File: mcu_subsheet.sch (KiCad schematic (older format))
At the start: 22 parts

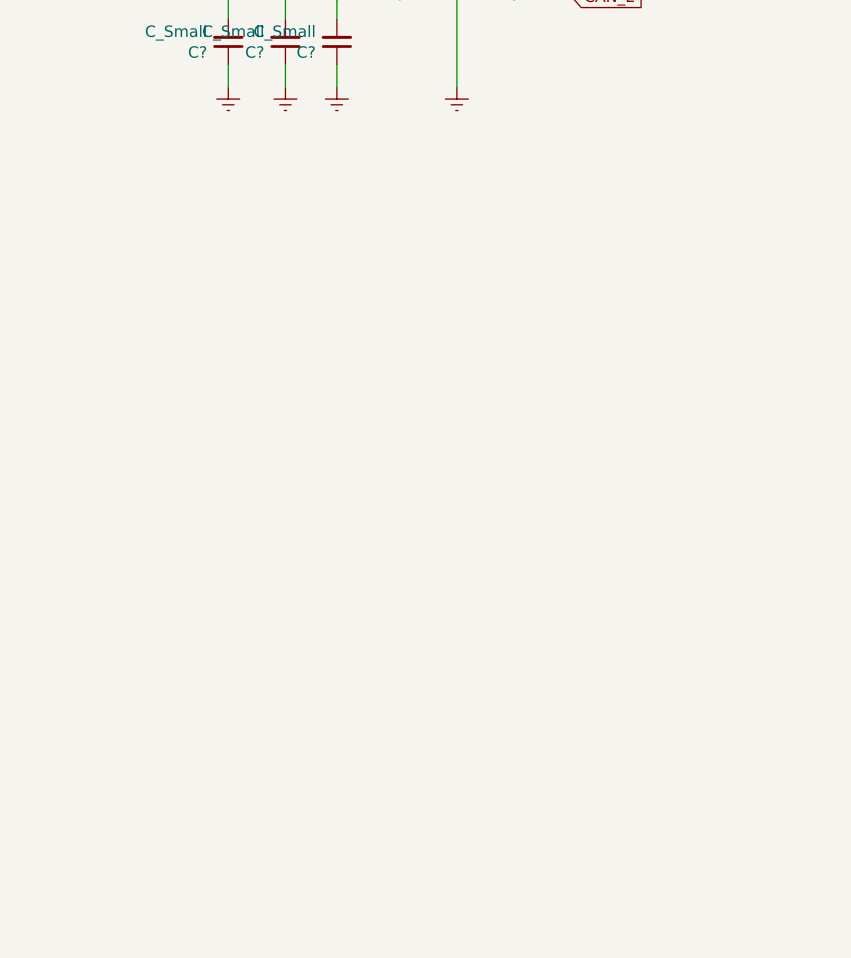
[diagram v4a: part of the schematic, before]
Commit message: [debug]: add swd connector
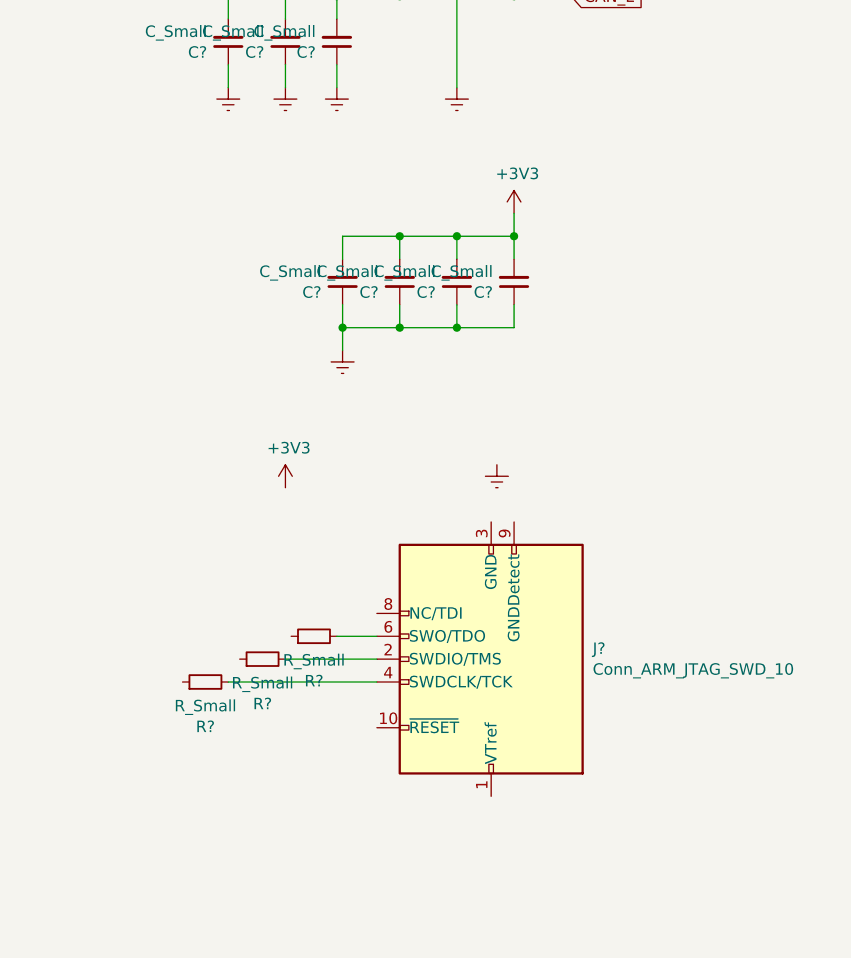
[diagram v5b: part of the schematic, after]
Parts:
- added C? (x4): C_Small, symbol Device:C_Small
- added J?: Conn_ARM_JTAG_SWD_10, symbol Connector:Conn_ARM_JTAG_SWD_10
- added R? (x3): R_Small, symbol Device:R_Small
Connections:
- net +3V3: now also C?.2, C?.2, C?.2, C?.2
- net Earth: now also C?.1, C?.1, C?.1, C?.1
- new net: J?.2 (SWDIO/TMS), R?.2
- new net: J?.3 (GND), J?.5 (GND)
- new net: J?.4 (SWDCLK/TCK), R?.2
- new net: J?.6 (SWO/TDO), R?.2
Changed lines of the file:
@@
 Wire Wire Line
 	7150 2050 7150 2150
+$Comp
+L Connector:Conn_ARM_JTAG_SWD_10 J?
+U 1 1 61E3A5F4
+P 9650 4750
+F 0 "J?" H 9206 4704 50  0000 R CNN
+F 1 "Conn_ARM_JTAG_SWD_10" H 9206 4795 50  0000 R CNN
+F 2 "" H 9650 4750 50  0001 C CNN
+F 3 "http://infocenter.arm.com/help/topic/com.arm.doc.ddi0314h/DDI0314H_coresight_components_trm.pdf" V 9300 3500 50  0001 C CNN
+	1    9650 4750
+	-1   0    0    1
+$EndComp
+$Comp
+L power:+3V3 #PWR?
+U 1 1 61E4B09B
+P 8750 4000
+F 0 "#PWR?" H 8750 3850 50  0001 C CNN
+F 1 "+3V3" H 8765 4173 50  0000 C CNN
+F 2 "" H 8750 4000 50  0001 C CNN
+F 3 "" H 8750 4000 50  0001 C CNN
+	1    8750 4000
+	1    0    0    -1
+$EndComp
+Wire Wire Line
+	8975 4650 9150 4650
+$Comp
+L Device:R_Small R?
+U 1 1 61E51799
+P 8875 4650
+F 0 "R?" V 8679 4650 50  0000 C CNN
+F 1 "R_Small" V 8770 4650 50  0000 C CNN
+F 2 "" H 8875 4650 50  0001 C CNN
+F 3 "~" H 8875 4650 50  0001 C CNN
+	1    8875 4650
+	0    -1   -1   0
+$EndComp
+Wire Wire Line
+	9150 4750 8750 4750
+Wire Wire Line
+	9150 4850 8500 4850
+$Comp
+L Device:R_Small R?
+U 1 1 61E5C0B5
+P 8650 4750
+F 0 "R?" V 8454 4750 50  0000 C CNN
+F 1 "R_Small" V 8545 4750 50  0000 C CNN
+F 2 "" H 8650 4750 50  0001 C CNN
+F 3 "~" H 8650 4750 50  0001 C CNN
+	1    8650 4750
+	0    -1   -1   0
+$EndComp
+$Comp
+L Device:R_Small R?
+U 1 1 61E5C7BA
+P 8400 4850
+F 0 "R?" V 8204 4850 50  0000 C CNN
+F 1 "R_Small" V 8295 4850 50  0000 C CNN
+F 2 "" H 8400 4850 50  0001 C CNN
+F 3 "~" H 8400 4850 50  0001 C CNN
+	1    8400 4850
+	0    -1   -1   0
+$EndComp
+$Comp
+L power:+3V3 #PWR?
+U 1 1 61E5E40F
+P 9750 2800
+F 0 "#PWR?" H 9750 2650 50  0001 C CNN
+F 1 "+3V3" H 9765 2973 50  0000 C CNN
+F 2 "" H 9750 2800 50  0001 C CNN
+F 3 "" H 9750 2800 50  0001 C CNN
+	1    9750 2800
+	1    0    0    -1
+$EndComp
+$Comp
+L power:Earth #PWR?
+U 1 1 61E60ACE
+P 9000 3400
+F 0 "#PWR?" H 9000 3150 50  0001 C CNN
+F 1 "Earth" H 9000 3250 50  0001 C CNN
+F 2 "" H 9000 3400 50  0001 C CNN
+F 3 "~" H 9000 3400 50  0001 C CNN
+	1    9000 3400
+	1    0    0    -1
+$EndComp
+$Comp
+L Device:C_Small C?
+U 1 1 61E61CB9
+P 9500 3100
+F 0 "C?" H 9592 3146 50  0000 L CNN
+F 1 "C_Small" H 9592 3055 50  0000 L CNN
+F 2 "" H 9500 3100 50  0001 C CNN
+F 3 "~" H 9500 3100 50  0001 C CNN
+	1    9500 3100
+	-1   0    0    1
+$EndComp
+$Comp
+L Device:C_Small C?
+U 1 1 61E64D96
+P 9000 3100
+F 0 "C?" H 9092 3146 50  0000 L CNN
+F 1 "C_Small" H 9092 3055 50  0000 L CNN
+F 2 "" H 9000 3100 50  0001 C CNN
+F 3 "~" H 9000 3100 50  0001 C CNN
+	1    9000 3100
+	-1   0    0    1
+$EndComp
+$Comp
+L Device:C_Small C?
+U 1 1 61E667D6
+P 9250 3100
+F 0 "C?" H 9342 3146 50  0000 L CNN
+F 1 "C_Small" H 9342 3055 50  0000 L CNN
+F 2 "" H 9250 3100 50  0001 C CNN
+F 3 "~" H 9250 3100 50  0001 C CNN
+	1    9250 3100
+	-1   0    0    1
+$EndComp
+$Comp
+L Device:C_Small C?
+U 1 1 61E66B17
+P 9750 3100
+F 0 "C?" H 9842 3146 50  0000 L CNN
+F 1 "C_Small" H 9842 3055 50  0000 L CNN
+F 2 "" H 9750 3100 50  0001 C CNN
+F 3 "~" H 9750 3100 50  0001 C CNN
+	1    9750 3100
+	-1   0    0    1
+$EndComp
+Wire Wire Line
+	9000 3000 9000 2900
+Wire Wire Line
+	9000 2900 9250 2900
+Wire Wire Line
+	9250 2900 9250 3000
+Wire Wire Line
+	9250 2900 9500 2900
+Wire Wire Line
+	9500 2900 9500 3000
+Connection ~ 9250 2900
+Wire Wire Line
+	9750 3000 9750 2900
+Wire Wire Line
+	9750 2900 9500 2900
+Connection ~ 9500 2900
+Wire Wire Line
+	9500 3200 9500 3300
+Wire Wire Line
+	9500 3300 9750 3300
+Wire Wire Line
+	9750 3300 9750 3200
+Wire Wire Line
+	9500 3300 9250 3300
+Wire Wire Line
+	9250 3300 9250 3200
+Connection ~ 9500 3300
+Wire Wire Line
+	9000 3200 9000 3300
+Wire Wire Line
+	9000 3300 9250 3300
+Connection ~ 9250 3300
+Wire Wire Line
+	9000 3300 9000 3400
+Connection ~ 9000 3300
+Wire Wire Line
+	9750 2800 9750 2900
+Connection ~ 9750 2900
+$Comp
+L power:Earth #PWR?
+U 1 1 61E4A6B2
+P 9675 3900
+F 0 "#PWR?" H 9675 3650 50  0001 C CNN
+F 1 "Earth" H 9675 3750 50  0001 C CNN
+F 2 "" H 9675 3900 50  0001 C CNN
+F 3 "~" H 9675 3900 50  0001 C CNN
+	1    9675 3900
+	1    0    0    -1
+$EndComp
 $EndSCHEMATC

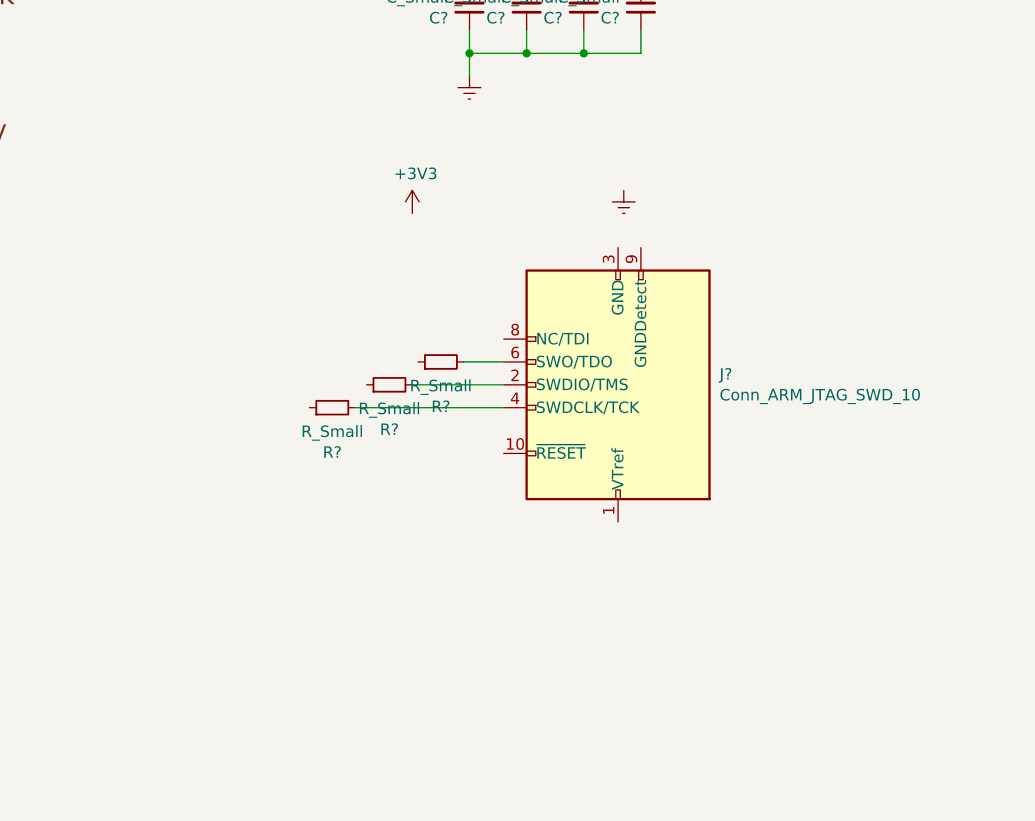
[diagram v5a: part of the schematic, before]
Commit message: [swd]: debug scheme updated (ARM-dev docs)
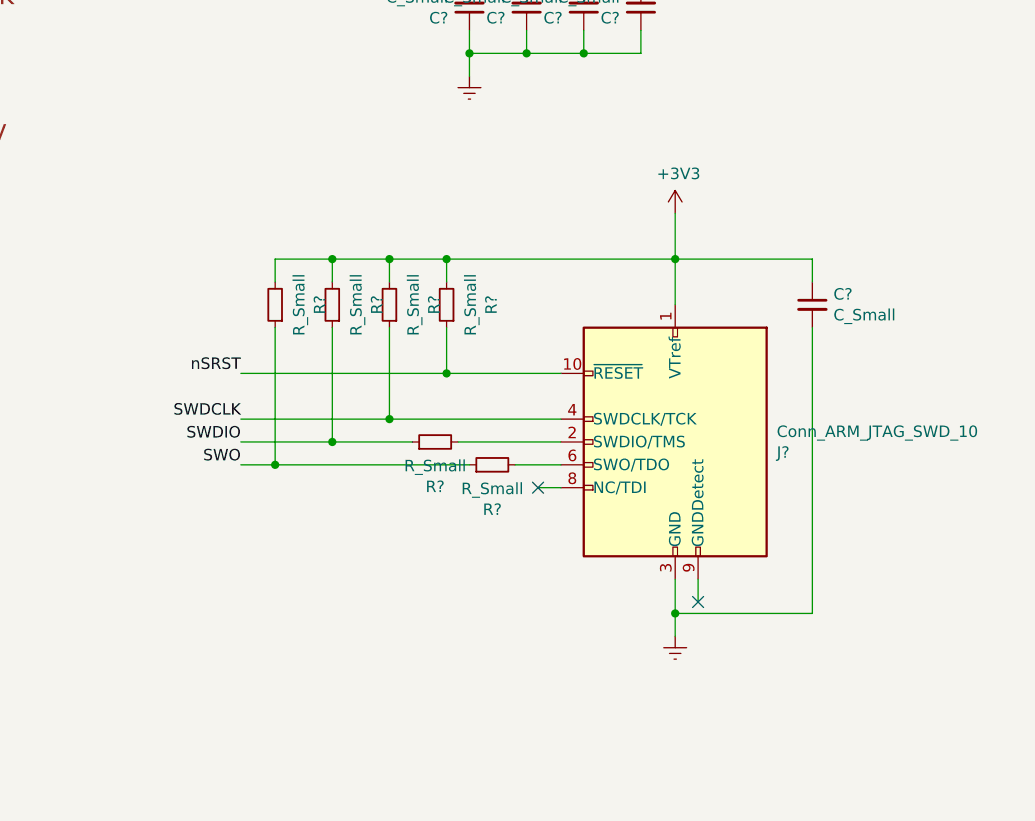
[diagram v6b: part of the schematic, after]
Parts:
- added C?: C_Small, symbol Device:C_Small
- added R? (x3): R_Small, symbol Device:R_Small
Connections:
- net +3V3: now also J?.1 (VTref), R?.2, C?.1, R?.2, R?.2, R?.2
- net Earth: now also J?.3 (GND), J?.5 (GND), C?.2
- net nSRST: now reaches J?.10 (~RESET~)
- net nSRST: now also R?.1
- net at J?.2 (SWDIO/TMS): now also R?.2; no longer R?.2
- net SWDCLK: now reaches J?.4 (SWDCLK/TCK)
- net SWDCLK: now also R?.1; no longer R?.2
- net SWO: now reaches R?.1
- net SWO: now also R?.1
- net SWDIO: now reaches R?.1
- net SWDIO: now also R?.1
- no-connect marks 0 -> 2
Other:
- moved on the sheet: J?, R?
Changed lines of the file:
@@
 	7150 2050 7150 2150
-$Comp
-L Connector:Conn_ARM_JTAG_SWD_10 J?
-U 1 1 61E3A5F4
-P 9650 4750
-F 0 "J?" H 9206 4704 50  0000 R CNN
-F 1 "Conn_ARM_JTAG_SWD_10" H 9206 4795 50  0000 R CNN
-F 2 "" H 9650 4750 50  0001 C CNN
-F 3 "http://infocenter.arm.com/help/topic/com.arm.doc.ddi0314h/DDI0314H_coresight_components_trm.pdf" V 9300 3500 50  0001 C CNN
-	1    9650 4750
-	-1   0    0    1
-$EndComp
-$Comp
-L power:+3V3 #PWR?
-U 1 1 61E4B09B
-P 8750 4000
-F 0 "#PWR?" H 8750 3850 50  0001 C CNN
-F 1 "+3V3" H 8765 4173 50  0000 C CNN
-F 2 "" H 8750 4000 50  0001 C CNN
-F 3 "" H 8750 4000 50  0001 C CNN
-	1    8750 4000
-	1    0    0    -1
-$EndComp
-Wire Wire Line
-	8975 4650 9150 4650
-$Comp
-L Device:R_Small R?
-U 1 1 61E51799
-P 8875 4650
-F 0 "R?" V 8679 4650 50  0000 C CNN
-F 1 "R_Small" V 8770 4650 50  0000 C CNN
-F 2 "" H 8875 4650 50  0001 C CNN
-F 3 "~" H 8875 4650 50  0001 C CNN
-	1    8875 4650
-	0    -1   -1   0
-$EndComp
-Wire Wire Line
-	9150 4750 8750 4750
-Wire Wire Line
-	9150 4850 8500 4850
-$Comp
-L Device:R_Small R?
-U 1 1 61E5C0B5
-P 8650 4750
-F 0 "R?" V 8454 4750 50  0000 C CNN
-F 1 "R_Small" V 8545 4750 50  0000 C CNN
-F 2 "" H 8650 4750 50  0001 C CNN
-F 3 "~" H 8650 4750 50  0001 C CNN
-	1    8650 4750
-	0    -1   -1   0
-$EndComp
-$Comp
-L Device:R_Small R?
-U 1 1 61E5C7BA
-P 8400 4850
-F 0 "R?" V 8204 4850 50  0000 C CNN
-F 1 "R_Small" V 8295 4850 50  0000 C CNN
-F 2 "" H 8400 4850 50  0001 C CNN
-F 3 "~" H 8400 4850 50  0001 C CNN
-	1    8400 4850
-	0    -1   -1   0
-$EndComp
 $Comp
 L power:+3V3 #PWR?
@@
 	9750 2800 9750 2900
 Connection ~ 9750 2900
+Wire Wire Line
+	8150 5100 9000 5100
+Connection ~ 8150 5100
+Wire Wire Line
+	8150 4500 8150 5100
+Wire Wire Line
+	8400 4500 8400 5000
+Wire Wire Line
+	8400 5000 8750 5000
+Connection ~ 8400 5000
+Connection ~ 8650 4900
+Wire Wire Line
+	8650 4500 8650 4900
+Wire Wire Line
+	8900 4700 9400 4700
+Connection ~ 8900 4700
+Wire Wire Line
+	8900 4500 8900 4700
+Wire Wire Line
+	8000 4900 8650 4900
+Wire Wire Line
+	8000 5100 8150 5100
+$Comp
+L Device:R_Small R?
+U 1 1 61E51799
+P 9100 5100
+F 0 "R?" V 8904 5100 50  0000 C CNN
+F 1 "R_Small" V 8995 5100 50  0000 C CNN
+F 2 "" H 9100 5100 50  0001 C CNN
+F 3 "~" H 9100 5100 50  0001 C CNN
+	1    9100 5100
+	0    -1   -1   0
+$EndComp
+Wire Wire Line
+	9200 5100 9400 5100
+Text Label 8000 5100 2    50   ~ 0
+SWO
+Text Label 8000 5000 2    50   ~ 0
+SWDIO
+Wire Wire Line
+	8000 5000 8400 5000
+Wire Wire Line
+	8000 4700 8900 4700
+NoConn ~ 10000 5700
+Wire Wire Line
+	10000 5700 10000 5600
+Wire Wire Line
+	10500 4200 10500 4300
+Wire Wire Line
+	9900 4200 10500 4200
+Wire Wire Line
+	9900 5750 9900 5850
+Connection ~ 9900 5750
+Wire Wire Line
+	10500 5750 10500 4500
+Wire Wire Line
+	9900 5750 10500 5750
+Wire Wire Line
+	9900 5600 9900 5750
+Wire Wire Line
+	9900 4200 9900 4400
+Connection ~ 9900 4200
+Connection ~ 8900 4200
+Wire Wire Line
+	8900 4200 9900 4200
+Wire Wire Line
+	9900 4000 9900 4200
+Text Label 8000 4700 2    50   ~ 0
+nSRST
+Text Label 8000 4900 2    50   ~ 0
+SWDCLK
+Wire Wire Line
+	8150 4300 8150 4200
+$Comp
+L Device:R_Small R?
+U 1 1 6200D08A
+P 8150 4400
+F 0 "R?" V 7954 4400 50  0000 C CNN
+F 1 "R_Small" V 8045 4400 50  0000 C CNN
+F 2 "" H 8150 4400 50  0001 C CNN
+F 3 "~" H 8150 4400 50  0001 C CNN
+	1    8150 4400
+	-1   0    0    1
+$EndComp
+Connection ~ 8400 4200
+Wire Wire Line
+	8150 4200 8400 4200
+Wire Wire Line
+	8650 4200 8900 4200
+Connection ~ 8650 4200
+Wire Wire Line
+	8650 4300 8650 4200
+Wire Wire Line
+	8400 4200 8650 4200
+$Comp
+L Device:R_Small R?
+U 1 1 61FB4CB2
+P 8650 4400
+F 0 "R?" V 8454 4400 50  0000 C CNN
+F 1 "R_Small" V 8545 4400 50  0000 C CNN
+F 2 "" H 8650 4400 50  0001 C CNN
+F 3 "~" H 8650 4400 50  0001 C CNN
+	1    8650 4400
+	-1   0    0    1
+$EndComp
+NoConn ~ 9300 5200
+Wire Wire Line
+	9400 5200 9300 5200
+Wire Wire Line
+	8900 4300 8900 4200
+$Comp
+L Device:R_Small R?
+U 1 1 61F08319
+P 8900 4400
+F 0 "R?" V 8704 4400 50  0000 C CNN
+F 1 "R_Small" V 8795 4400 50  0000 C CNN
+F 2 "" H 8900 4400 50  0001 C CNN
+F 3 "~" H 8900 4400 50  0001 C CNN
+	1    8900 4400
+	-1   0    0    1
+$EndComp
+Wire Wire Line
+	8400 4300 8400 4200
+$Comp
+L Device:C_Small C?
+U 1 1 61EC2D58
+P 10500 4400
+F 0 "C?" H 10592 4446 50  0000 L CNN
+F 1 "C_Small" H 10592 4355 50  0000 L CNN
+F 2 "" H 10500 4400 50  0001 C CNN
+F 3 "~" H 10500 4400 50  0001 C CNN
+	1    10500 4400
+	1    0    0    -1
+$EndComp
+$Comp
+L Connector:Conn_ARM_JTAG_SWD_10 J?
+U 1 1 61E3A5F4
+P 9900 5000
+F 0 "J?" H 9456 4954 50  0000 R CNN
+F 1 "Conn_ARM_JTAG_SWD_10" H 9456 5045 50  0000 R CNN
+F 2 "" H 9900 5000 50  0001 C CNN
+F 3 "http://infocenter.arm.com/help/topic/com.arm.doc.ddi0314h/DDI0314H_coresight_components_trm.pdf" V 9550 3750 50  0001 C CNN
+	1    9900 5000
+	-1   0    0    -1
+$EndComp
+$Comp
+L Device:R_Small R?
+U 1 1 61E5C0B5
+P 8400 4400
+F 0 "R?" V 8204 4400 50  0000 C CNN
+F 1 "R_Small" V 8295 4400 50  0000 C CNN
+F 2 "" H 8400 4400 50  0001 C CNN
+F 3 "~" H 8400 4400 50  0001 C CNN
+	1    8400 4400
+	-1   0    0    1
+$EndComp
+$Comp
+L Device:R_Small R?
+U 1 1 61E5C7BA
+P 8850 5000
+F 0 "R?" V 8654 5000 50  0000 C CNN
+F 1 "R_Small" V 8745 5000 50  0000 C CNN
+F 2 "" H 8850 5000 50  0001 C CNN
+F 3 "~" H 8850 5000 50  0001 C CNN
+	1    8850 5000
+	0    -1   -1   0
+$EndComp
 $Comp
 L power:Earth #PWR?
 U 1 1 61E4A6B2
-P 9675 3900
-F 0 "#PWR?" H 9675 3650 50  0001 C CNN
-F 1 "Earth" H 9675 3750 50  0001 C CNN
-F 2 "" H 9675 3900 50  0001 C CNN
-F 3 "~" H 9675 3900 50  0001 C CNN
-	1    9675 3900
-	1    0    0    -1
-$EndComp
+P 9900 5850
+F 0 "#PWR?" H 9900 5600 50  0001 C CNN
+F 1 "Earth" H 9900 5700 50  0001 C CNN
+F 2 "" H 9900 5850 50  0001 C CNN
+F 3 "~" H 9900 5850 50  0001 C CNN
+	1    9900 5850
+	1    0    0    -1
+$EndComp
+$Comp
+L power:+3V3 #PWR?
+U 1 1 61E4B09B
+P 9900 4000
+F 0 "#PWR?" H 9900 3850 50  0001 C CNN
+F 1 "+3V3" H 9915 4173 50  0000 C CNN
+F 2 "" H 9900 4000 50  0001 C CNN
+F 3 "" H 9900 4000 50  0001 C CNN
+	1    9900 4000
+	1    0    0    -1
+$EndComp
+Wire Wire Line
+	8950 5000 9400 5000
+Wire Wire Line
+	8650 4900 9400 4900
 $EndSCHEMATC
